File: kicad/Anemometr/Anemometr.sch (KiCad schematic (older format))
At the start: 158 parts, among them J1 Conn_01x01_Female, J10 +Z3, J11 -Z3, J12 +Z4, J13 -Z4, J14 SWD, J15 SWC, J16 Z4, J17 Z4, J18 1 TxD+, J19 2 TxD-, J2 Conn_01x01_Female, J20 3 RxD+, J21 4, J22 5, J23 6 RxD-, J24 7, J25 8, J26 Z4, J27 Z4, J28 Z4, J29 Z4, J3 RST, J30 Z4, J31 Z4, J32 Z4, J33 Z4, J34 Z4, J35 Z4, J4 TxD, J5 RxD, J6 +Z1, J7 -Z1, J8 +Z2, J9 -Z2, U1 TS5A3166DBVR, U10 MCP1700-3002E, U2 LMV7239, U3 TS5A3166DBVR, U4 TS5A3166DBVR, U5 STM32F103C8Tx, U6 TS5A3166DBVR, U7 LM2734Y, U8 MCP1700-5002E, U9 MCP1700-3002E, Y1 8MHz, Y2 25MHz

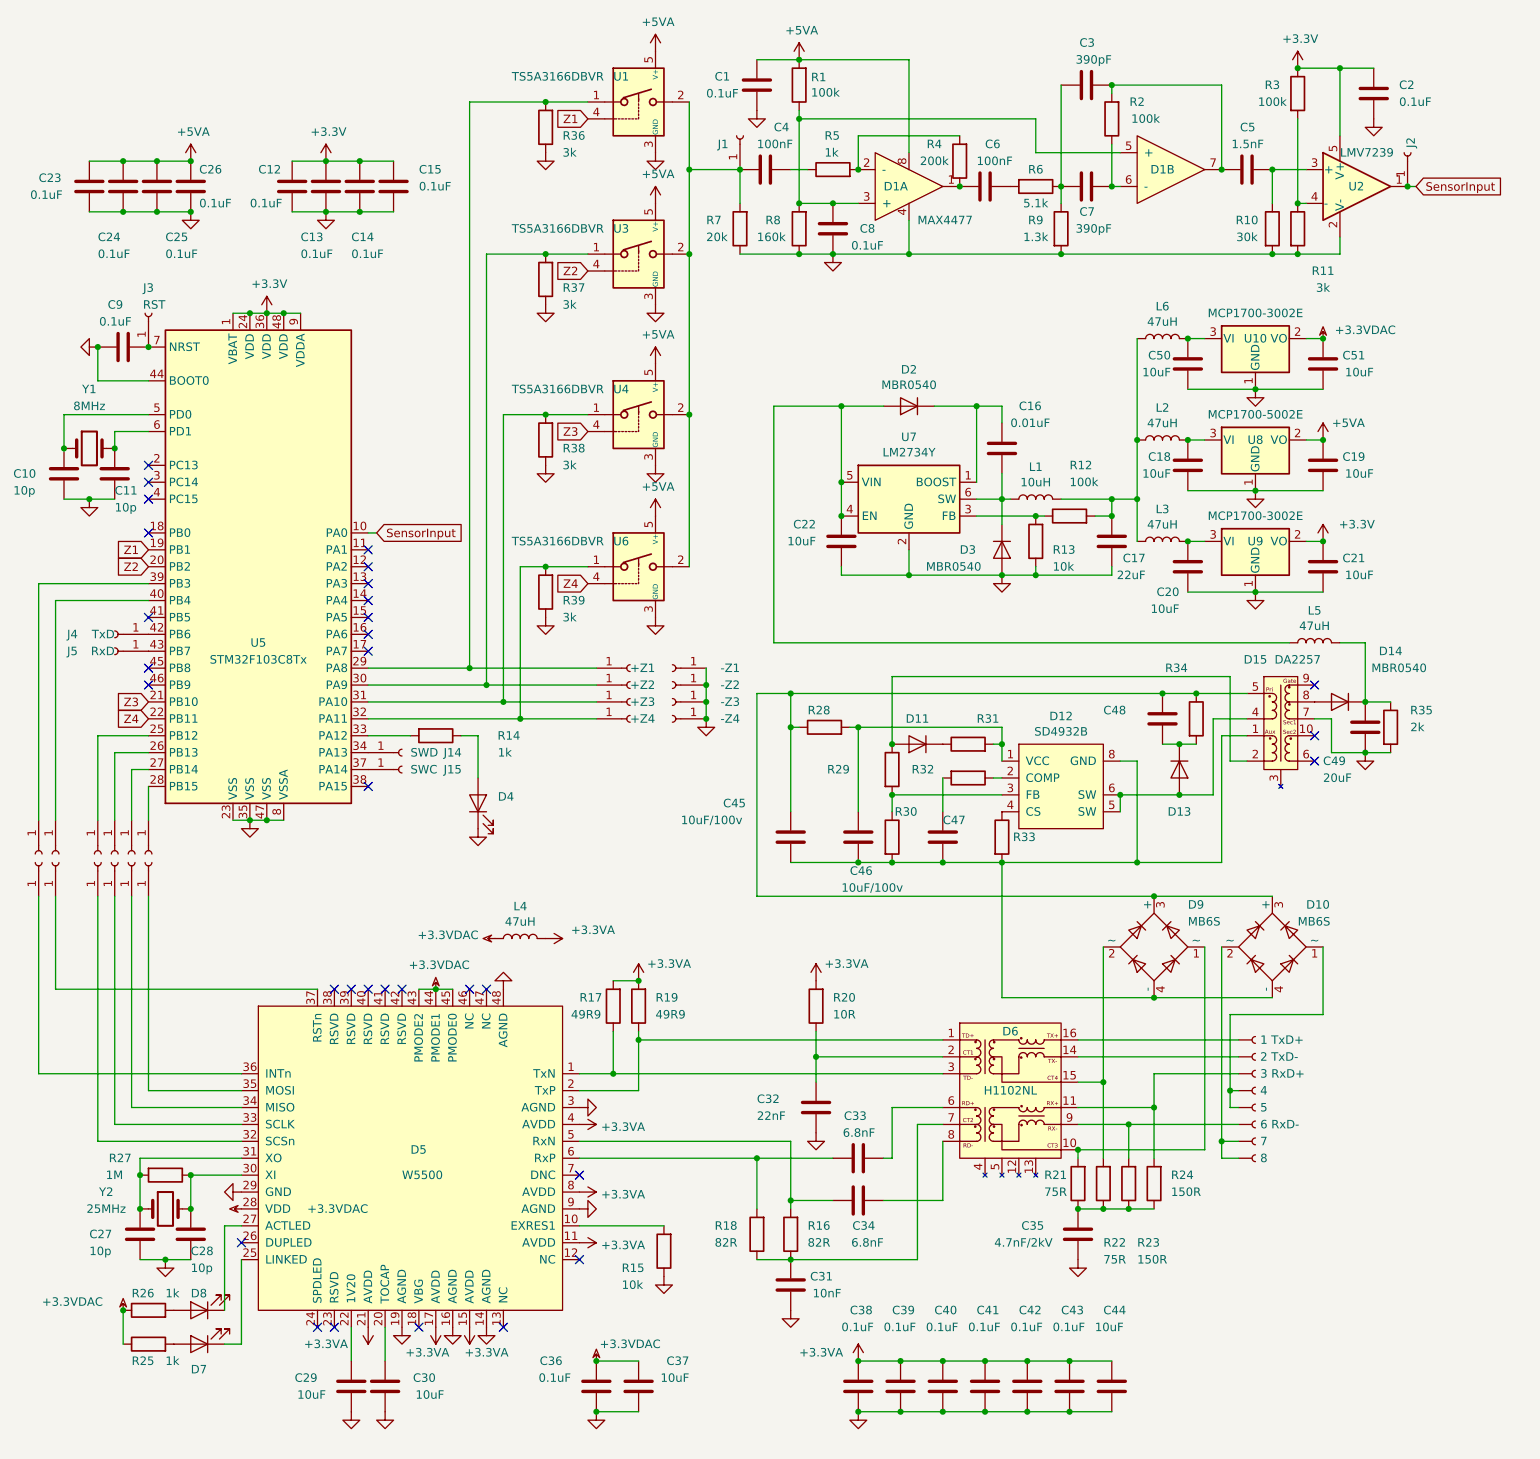
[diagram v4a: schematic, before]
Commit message: изменено:      kicad/Anemometr/Anemometr.kicad_pcb 	изменено:      kicad/Anemometr/Anemometr.kicad_pcb-bak 	изменено:      kicad/Anemometr/Anemometr.sch 	изменено:      kicad/Anemometr/Anemometr.sch-bak
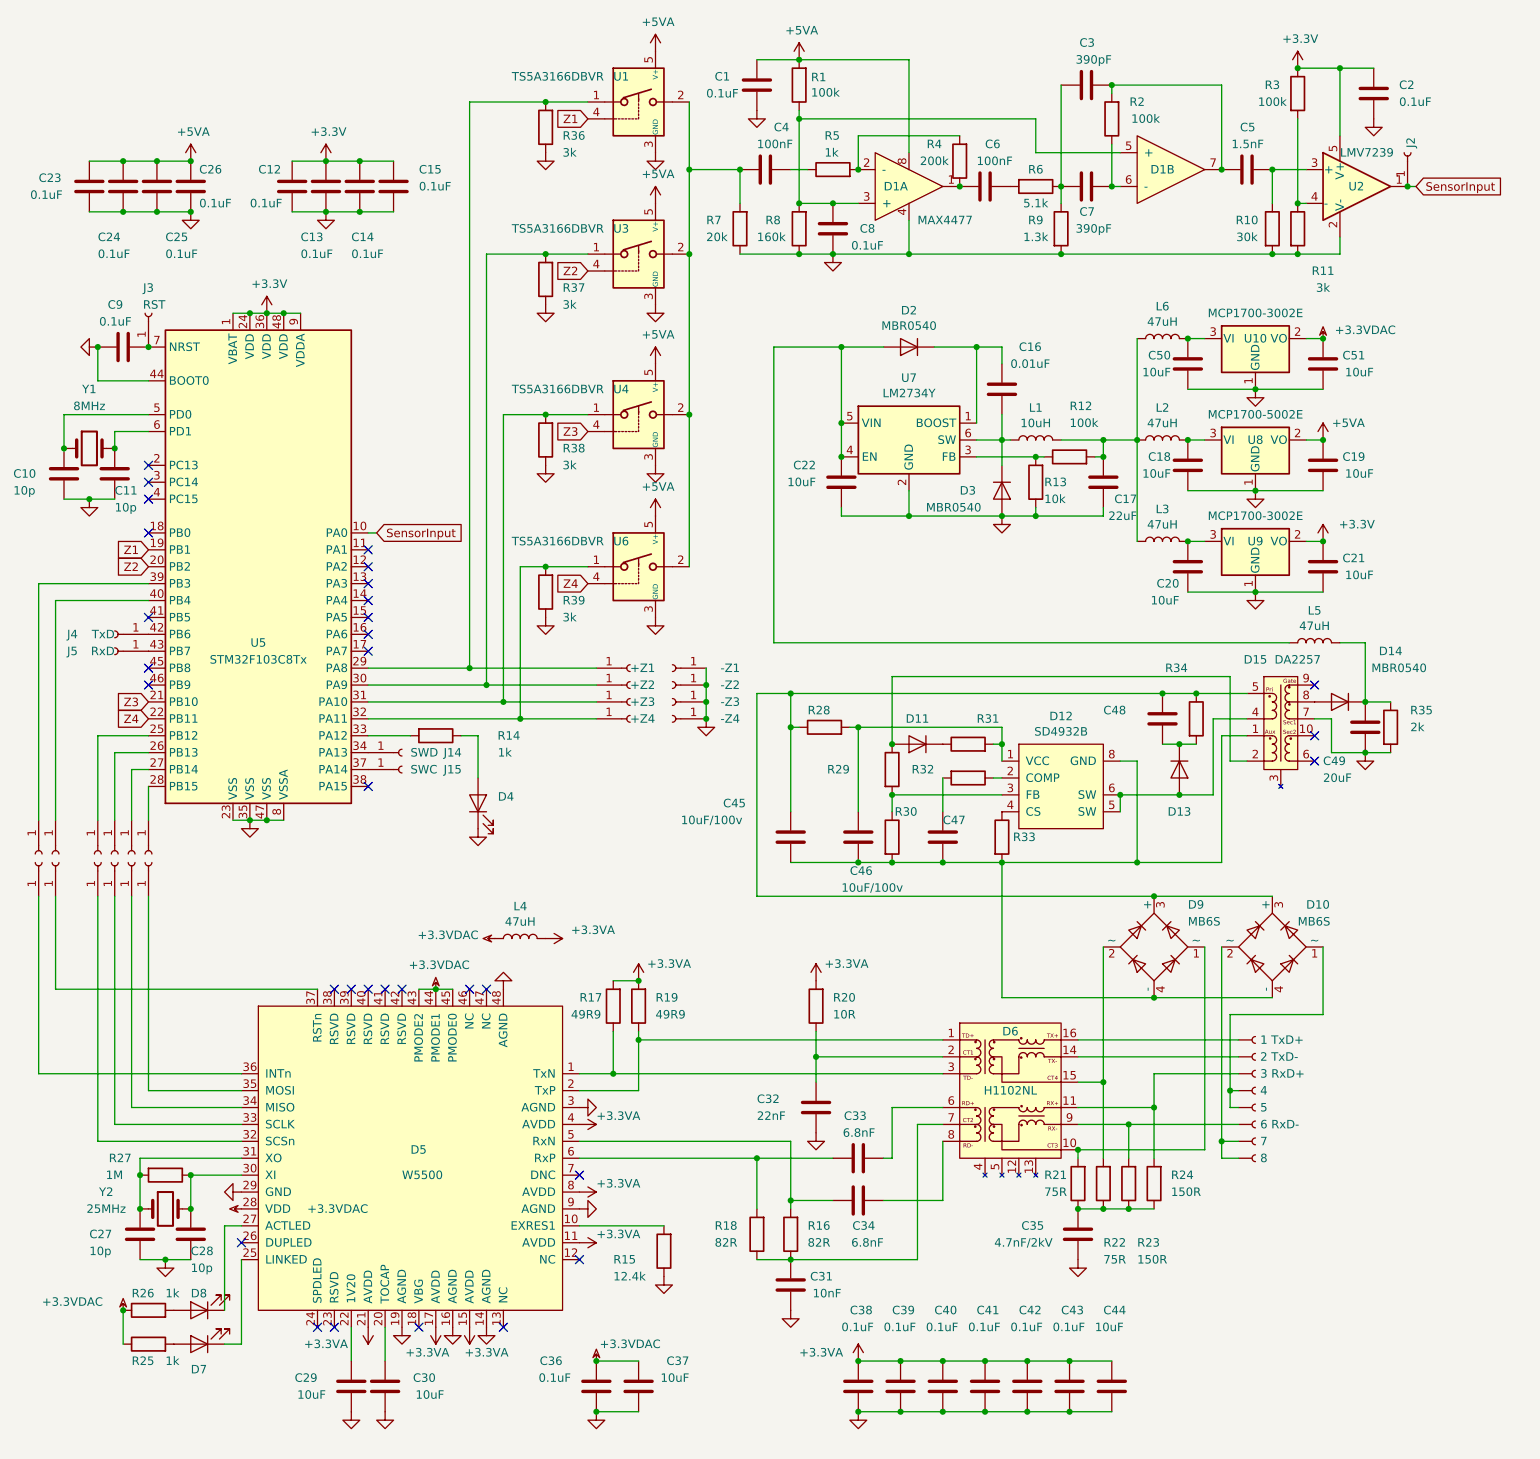
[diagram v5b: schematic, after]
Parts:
- removed J1: Conn_01x01_Female, My-library:SMD-CONN, symbol Connector:Conn_01x01_Female
- R1: footprint Resistor_SMD:R_0805_2012Metric -> Resistor_SMD:R_0603_1608Metric
- R15: value 10k -> 12.4k
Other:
- moved on the sheet: C16, C17, C22, D2, D3, L1, R12, R13, U7
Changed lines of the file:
@@
 F 0 "R1" H 8230 1554 50  0000 R CNN
 F 1 "100k" H 8230 1645 50  0000 R CNN
-F 2 "Resistor_SMD:R_0805_2012Metric" V 8230 1600 50  0001 C CNN
+F 2 "Resistor_SMD:R_0603_1608Metric" V 8230 1600 50  0001 C CNN
 F 3 "~" H 8300 1600 50  0001 C CNN
 	1    8300 1600
@@
 $EndComp
 $Comp
-L Connector:Conn_01x01_Female J1
-U 1 1 61CFD143
-P 7950 1900
-F 0 "J1" V 7900 2000 50  0000 C CNN
-F 1 "Conn_01x01_Female" H 7978 1835 50  0001 L CNN
-F 2 "My-library:SMD-CONN" H 7950 1900 50  0001 C CNN
-F 3 "~" H 7950 1900 50  0001 C CNN
-	1    7950 1900
-	0    -1   -1   0
-$EndComp
-$Comp
 L Device:C C4
 U 1 1 61D227BC
@@
 L Regulator_Switching:LM2734Y U7
 U 1 1 61D61AAE
-P 8950 4050
-F 0 "U7" H 8950 4417 50  0000 C CNN
-F 1 "LM2734Y" H 8950 4326 50  0000 C CNN
-F 2 "Package_TO_SOT_SMD:TSOT-23-6" H 8975 3800 50  0001 L CIN
-F 3 "http://www.ti.com/lit/ds/symlink/lm2734.pdf" H 8850 4150 50  0001 C CNN
-	1    8950 4050
+P 8950 3700
+F 0 "U7" H 8950 4067 50  0000 C CNN
+F 1 "LM2734Y" H 8950 3976 50  0000 C CNN
+F 2 "Package_TO_SOT_SMD:TSOT-23-6" H 8975 3450 50  0001 L CIN
+F 3 "http://www.ti.com/lit/ds/symlink/lm2734.pdf" H 8850 3800 50  0001 C CNN
+	1    8950 3700
 	1    0    0    -1
 $EndComp
@@
 L Device:D D2
 U 1 1 61D6A2C4
-P 8950 3500
-F 0 "D2" H 8950 3284 50  0000 C CNN
-F 1 "MBR0540" H 8950 3375 50  0000 C CNN
-F 2 "Diode_SMD:D_SOD-123" H 8950 3500 50  0001 C CNN
-F 3 "~" H 8950 3500 50  0001 C CNN
-	1    8950 3500
+P 8950 3150
+F 0 "D2" H 8950 2934 50  0000 C CNN
+F 1 "MBR0540" H 8950 3025 50  0000 C CNN
+F 2 "Diode_SMD:D_SOD-123" H 8950 3150 50  0001 C CNN
+F 3 "~" H 8950 3150 50  0001 C CNN
+	1    8950 3150
 	-1   0    0    1
 $EndComp
@@
 L Device:C C17
 U 1 1 61D6B87F
-P 10150 4300
-F 0 "C17" H 9950 4400 50  0000 L CNN
-F 1 "22uF" H 9950 4500 50  0000 L CNN
-F 2 "Capacitor_SMD:C_0805_2012Metric" H 10188 4150 50  0001 C CNN
-F 3 "~" H 10150 4300 50  0001 C CNN
-	1    10150 4300
+P 10100 3950
+F 0 "C17" H 9900 4050 50  0000 L CNN
+F 1 "22uF" H 9900 4150 50  0000 L CNN
+F 2 "Capacitor_SMD:C_0805_2012Metric" H 10138 3800 50  0001 C CNN
+F 3 "~" H 10100 3950 50  0001 C CNN
+	1    10100 3950
 	-1   0    0    1
 $EndComp
@@
 L Device:R R13
 U 1 1 61D6C02B
-P 9700 4300
-F 0 "R13" H 9600 4350 50  0000 R CNN
-F 1 "10k" H 9600 4450 50  0000 R CNN
-F 2 "Resistor_SMD:R_0805_2012Metric" V 9630 4300 50  0001 C CNN
-F 3 "~" H 9700 4300 50  0001 C CNN
-	1    9700 4300
+P 9700 3950
+F 0 "R13" H 9650 3950 50  0000 R CNN
+F 1 "10k" H 9650 4050 50  0000 R CNN
+F 2 "Resistor_SMD:R_0805_2012Metric" V 9630 3950 50  0001 C CNN
+F 3 "~" H 9700 3950 50  0001 C CNN
+	1    9700 3950
 	-1   0    0    1
 $EndComp
@@
 L Device:L L1
 U 1 1 61D6CE9C
-P 9700 4050
-F 0 "L1" V 9890 4050 50  0000 C CNN
-F 1 "10uH" V 9799 4050 50  0000 C CNN
-F 2 "Inductor_SMD:L_1812_4532Metric" H 9700 4050 50  0001 C CNN
-F 3 "~" H 9700 4050 50  0001 C CNN
-	1    9700 4050
+P 9700 3700
+F 0 "L1" V 9890 3700 50  0000 C CNN
+F 1 "10uH" V 9799 3700 50  0000 C CNN
+F 2 "Inductor_SMD:L_1812_4532Metric" H 9700 3700 50  0001 C CNN
+F 3 "~" H 9700 3700 50  0001 C CNN
+	1    9700 3700
 	0    -1   -1   0
 $EndComp
@@
 L power:GND #PWR019
 U 1 1 61D6DC00
-P 9500 4500
-F 0 "#PWR019" H 9500 4250 50  0001 C CNN
-F 1 "GND" H 9505 4327 50  0001 C CNN
-F 2 "" H 9500 4500 50  0001 C CNN
-F 3 "" H 9500 4500 50  0001 C CNN
-	1    9500 4500
+P 9500 4150
+F 0 "#PWR019" H 9500 3900 50  0001 C CNN
+F 1 "GND" H 9505 3977 50  0001 C CNN
+F 2 "" H 9500 4150 50  0001 C CNN
+F 3 "" H 9500 4150 50  0001 C CNN
+	1    9500 4150
 	1    0    0    -1
 $EndComp
 Wire Wire Line
-	8550 4150 8550 3950
+	8550 3800 8550 3600
 Wire Wire Line
-	8550 3950 8550 3500
+	8550 3600 8550 3150
 Wire Wire Line
-	8550 3500 8800 3500
-Connection ~ 8550 3950
+	8550 3150 8800 3150
+Connection ~ 8550 3600
 Wire Wire Line
-	9350 3950 9350 3500
+	9350 3600 9350 3150
 Wire Wire Line
-	9350 3500 9100 3500
+	9350 3150 9100 3150
 Wire Wire Line
-	9350 4050 9500 4050
-Connection ~ 9500 4050
+	9350 3700 9500 3700
+Connection ~ 9500 3700
 Wire Wire Line
-	9500 4050 9550 4050
+	9500 3700 9550 3700
 Wire Wire Line
-	9500 3600 9500 3500
+	9500 3250 9500 3150
 Wire Wire Line
-	9500 3500 9350 3500
-Connection ~ 9350 3500
+	9500 3150 9350 3150
+Connection ~ 9350 3150
 $Comp
 L Device:D D3
 U 1 1 61D97E2F
-P 9500 4350
-F 0 "D3" V 9500 4100 50  0000 L CNN
-F 1 "MBR0540" V 9600 3900 50  0000 L CNN
-F 2 "Diode_SMD:D_SOD-123" H 9500 4350 50  0001 C CNN
-F 3 "~" H 9500 4350 50  0001 C CNN
-	1    9500 4350
+P 9500 4000
+F 0 "D3" V 9500 3750 50  0000 L CNN
+F 1 "MBR0540" V 9600 3550 50  0000 L CNN
+F 2 "Diode_SMD:D_SOD-123" H 9500 4000 50  0001 C CNN
+F 3 "~" H 9500 4000 50  0001 C CNN
+	1    9500 4000
 	0    1    1    0
 $EndComp
 Wire Wire Line
-	9500 4050 9500 4200
+	9500 3700 9500 3850
 Wire Wire Line
-	9500 4500 8950 4500
+	9500 4150 8950 4150
 Wire Wire Line
-	8950 4500 8950 4350
-Connection ~ 9500 4500
+	8950 4150 8950 4000
+Connection ~ 9500 4150
 $Comp
 L Device:R R12
 U 1 1 61DA4E2B
-P 9900 4150
-F 0 "R12" V 10200 4150 50  0000 R CNN
-F 1 "100k" V 10100 4150 50  0000 R CNN
-F 2 "Resistor_SMD:R_0805_2012Metric" V 9830 4150 50  0001 C CNN
-F 3 "~" H 9900 4150 50  0001 C CNN
-	1    9900 4150
+P 9900 3800
+F 0 "R12" V 10200 3800 50  0000 R CNN
+F 1 "100k" V 10100 3800 50  0000 R CNN
+F 2 "Resistor_SMD:R_0805_2012Metric" V 9830 3800 50  0001 C CNN
+F 3 "~" H 9900 3800 50  0001 C CNN
+	1    9900 3800
 	0    -1   -1   0
 $EndComp
 Wire Wire Line
-	9500 4500 9700 4500
-Wire Wire Line
-	9700 4500 9700 4450
-Wire Wire Line
-	9850 4050 10150 4050
-Wire Wire Line
-	10150 4050 10150 4150
+	9500 4150 9700 4150
 Wire Wire Line
-	10050 4150 10150 4150
-Connection ~ 10150 4150
+	9700 4150 9700 4100
 Wire Wire Line
-	9750 4150 9700 4150
-Connection ~ 9700 4150
-Wire Wire Line
-	9700 4150 9350 4150
-Wire Wire Line
-	9700 4500 10150 4500
+	9750 3800 9700 3800
+Connection ~ 9700 3800
 Wire Wire Line
-	10150 4500 10150 4450
-Connection ~ 9700 4500
+	9700 3800 9350 3800
 Connection ~ 7750 5350
 $Comp
@@
 $EndComp
 Wire Wire Line
-	8550 4500 8950 4500
-Connection ~ 8950 4500
+	8550 4150 8950 4150
+Connection ~ 8950 4150
 $Comp
 L Regulator_Linear:MCP1700-5002E_SOT23 U8
@@
 U 1 1 61E0DD64
 P 10600 4450
-F 0 "C20" H 10650 4600 50  0000 L CNN
-F 1 "10uF" H 10650 4700 50  0000 L CNN
+F 0 "C20" H 10650 4550 50  0000 L CNN
+F 1 "10uF" H 10650 4650 50  0000 L CNN
 F 2 "Capacitor_SMD:C_0805_2012Metric" H 10638 4300 50  0001 C CNN
 F 3 "~" H 10600 4450 50  0001 C CNN
@@
 	11300 4300 11400 4300
 Wire Wire Line
-	10150 4050 10300 4050
-Connection ~ 10150 4050
-Wire Wire Line
 	10600 4300 10700 4300
 Wire Wire Line
@@
 L Device:C C22
 U 1 1 61E9B6C6
-P 8550 4300
-F 0 "C22" H 8700 4200 50  0000 L CNN
-F 1 "10uF" H 8700 4300 50  0000 L CNN
-F 2 "Capacitor_SMD:C_0805_2012Metric" H 8588 4150 50  0001 C CNN
-F 3 "~" H 8550 4300 50  0001 C CNN
-	1    8550 4300
+P 8550 3950
+F 0 "C22" H 8700 3850 50  0000 L CNN
+F 1 "10uF" H 8700 3950 50  0000 L CNN
+F 2 "Capacitor_SMD:C_0805_2012Metric" H 8588 3800 50  0001 C CNN
+F 3 "~" H 8550 3950 50  0001 C CNN
+	1    8550 3950
 	-1   0    0    1
 $EndComp
-Connection ~ 8550 4150
+Connection ~ 8550 3800
 Wire Wire Line
-	8550 4450 8550 4500
+	8550 4100 8550 4150
 Wire Wire Line
 	6650 4450 6800 4450
@@
 P 7000 7750
 F 0 "#PWR040" H 7000 7600 50  0001 C CNN
-F 1 "+3.3VA" V 7015 7878 50  0000 L CNN
+F 1 "+3.3VA" V 6950 7850 50  0000 L CNN
 F 2 "" H 7000 7750 50  0001 C CNN
 F 3 "" H 7000 7750 50  0001 C CNN
@@
 P 7000 8150
 F 0 "#PWR041" H 7000 8000 50  0001 C CNN
-F 1 "+3.3VA" V 7015 8278 50  0000 L CNN
+F 1 "+3.3VA" V 6950 8250 50  0000 L CNN
 F 2 "" H 7000 8150 50  0001 C CNN
 F 3 "" H 7000 8150 50  0001 C CNN
@@
 P 7000 8450
 F 0 "#PWR043" H 7000 8300 50  0001 C CNN
-F 1 "+3.3VA" V 7015 8578 50  0000 L CNN
+F 1 "+3.3VA" V 6950 8550 50  0000 L CNN
 F 2 "" H 7000 8450 50  0001 C CNN
 F 3 "" H 7000 8450 50  0001 C CNN
@@
 U 1 1 61EF3C76
 P 7500 8500
-F 0 "R15" H 7750 8600 50  0000 R CNN
-F 1 "10k" H 7750 8700 50  0000 R CNN
+F 0 "R15" H 7800 8550 50  0000 R CNN
+F 1 "12.4k" H 7800 8650 50  0000 R CNN
 F 2 "Resistor_SMD:R_0402_1005Metric" V 7430 8500 50  0001 C CNN
 F 3 "~" H 7500 8500 50  0001 C CNN
@@
 Wire Wire Line
 	11650 4900 11650 5250
-Wire Wire Line
-	10300 4300 10300 4050
-Connection ~ 10300 4050
-Wire Wire Line
-	10300 4050 10300 3700
 $Comp
 L Regulator_Linear:MCP1700-3002E_SOT23 U10
@@
 L Device:C C16
 U 1 1 61D7B52F
-P 9500 3750
-F 0 "C16" H 9600 4000 50  0000 L CNN
-F 1 "0.01uF" H 9550 3900 50  0000 L CNN
-F 2 "Capacitor_SMD:C_0805_2012Metric" H 9538 3600 50  0001 C CNN
-F 3 "~" H 9500 3750 50  0001 C CNN
-	1    9500 3750
+P 9500 3400
+F 0 "C16" H 9600 3650 50  0000 L CNN
+F 1 "0.01uF" H 9550 3550 50  0000 L CNN
+F 2 "Capacitor_SMD:C_0805_2012Metric" H 9538 3250 50  0001 C CNN
+F 3 "~" H 9500 3400 50  0001 C CNN
+	1    9500 3400
 	1    0    0    -1
 $EndComp
 Wire Wire Line
-	9500 3900 9500 4050
+	9500 3550 9500 3700
 Connection ~ 3950 3750
 Connection ~ 4250 3750
@@
 	9700 1800 9700 2000
 Wire Wire Line
-	8150 3500 8550 3500
-Connection ~ 8550 3500
-Wire Wire Line
 	9950 7950 9950 7900
 Connection ~ 9950 7900
@@
 	9500 7000 10400 7000
 Wire Wire Line
-	8150 3500 8150 4900
-Wire Wire Line
 	8150 4900 11200 4900
 Wire Wire Line
@@
 Wire Wire Line
 	9150 5700 9150 5900
+Wire Wire Line
+	9850 3700 10100 3700
+Wire Wire Line
+	10050 3800 10100 3800
+Wire Wire Line
+	10100 3800 10100 3700
+Connection ~ 10100 3800
+Wire Wire Line
+	9700 4150 10100 4150
+Wire Wire Line
+	10100 4150 10100 4100
+Connection ~ 9700 4150
+Wire Wire Line
+	10300 3700 10300 4300
+Wire Wire Line
+	10100 3700 10300 3700
+Connection ~ 10100 3700
+Wire Wire Line
+	8150 3150 8550 3150
+Wire Wire Line
+	8150 3150 8150 4900
+Connection ~ 8550 3150
 $EndSCHEMATC
